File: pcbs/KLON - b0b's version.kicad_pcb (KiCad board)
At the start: 2 copper layers, 159.6 x 117.7 mm, 88 parts, among them J1 MJ-4PP-9, SW25 Rotary_Encoder_Switch

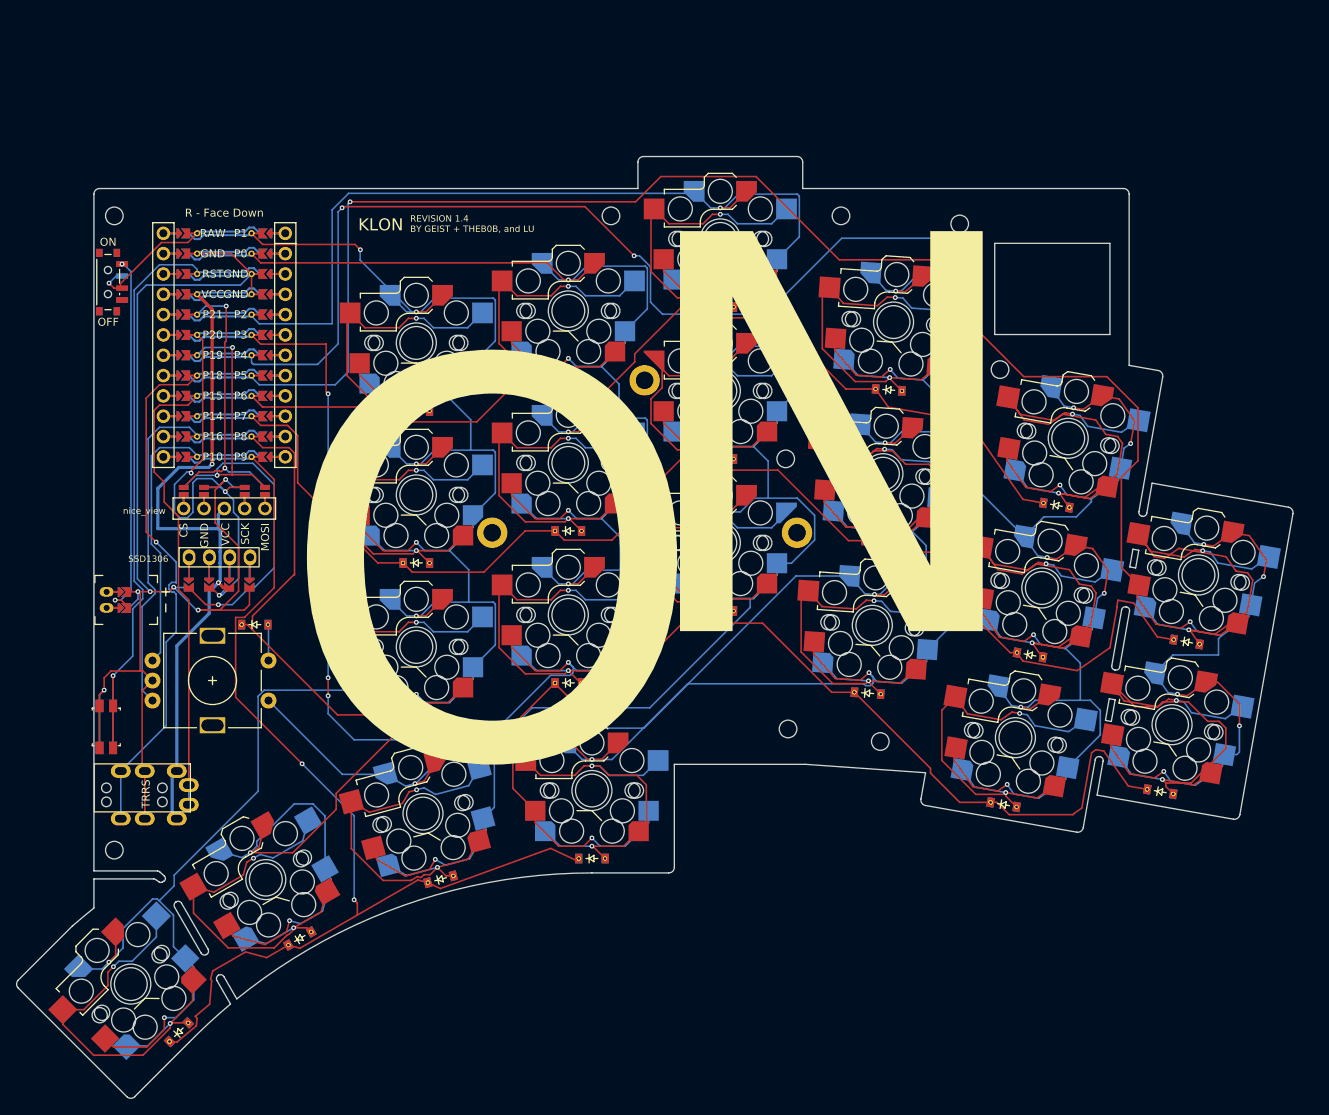
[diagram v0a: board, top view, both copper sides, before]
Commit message: rerouted diodes
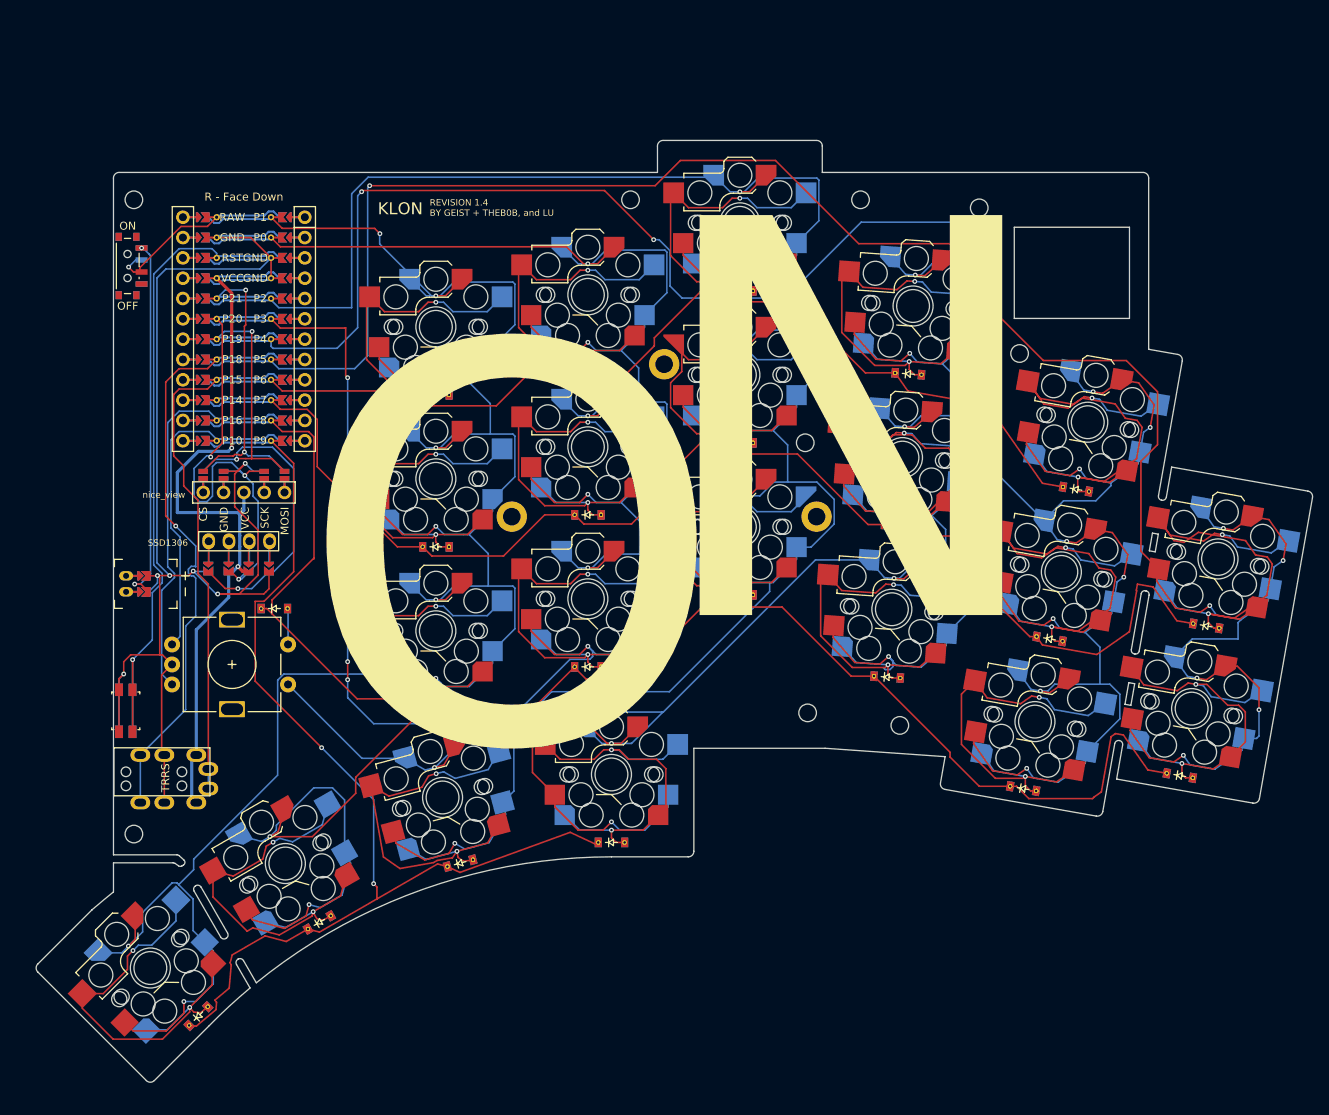
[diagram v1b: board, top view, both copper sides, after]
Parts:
- moved D20 3.16 mm to (161.9, 189.0)
- moved S30 3.16 mm to (214.5, 101.6)
- moved S9 3.16 mm to (214.5, 101.6)
- moved MH4 3.16 mm to (244.4, 99.7)
- moved JST1 3.16 mm to (137.7, 146.7)
- moved MH9 3.16 mm to (138.7, 178.0)
- moved S14 3.16 mm to (254.6, 145.2)
- moved S35 3.16 mm to (254.6, 145.2)
- moved S29 3.16 mm to (214.5, 120.6)
- moved S8 3.16 mm to (214.5, 120.6)
- moved S21 3.16 mm to (140.8, 194.7)
- moved S42 3.16 mm to (140.8, 194.7)
- moved D18 3.16 mm to (198.4, 179.0)
- moved MH1 3.16 mm to (138.7, 98.7)
- moved D4 3.16 mm to (195.5, 157.1)
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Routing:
- net col4: track 390.5 -> 360.6 mm
- net pinky_extra_bottom: track 63.5 -> 49.2 mm
- net pinky_top: track 64.5 -> 65.5 mm
- net index_top: track 52.8 -> 53.7 mm
- net 3_r0: track 53.5 -> 54.3 mm
- net middle_top: track 52.8 -> 53.6 mm
- net middle_home: track 53.6 -> 54.4 mm
- net ring_home: track 64.4 -> 65.2 mm
- net pinky_home: track 64.5 -> 65.3 mm
- net ring_bottom: track 52.8 -> 53.6 mm
- net 2_r0: track 53.7 -> 54.4 mm
- net inner_home: track 52.8 -> 53.5 mm
- net index_bottom: track 52.8 -> 53.4 mm
- net middle_bottom: track 52.8 -> 53.4 mm
- net 1_r0: track 48.6 -> 49.2 mm
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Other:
- outline, holes or cut-outs redrawn
